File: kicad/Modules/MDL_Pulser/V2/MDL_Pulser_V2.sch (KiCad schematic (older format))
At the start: 1 part

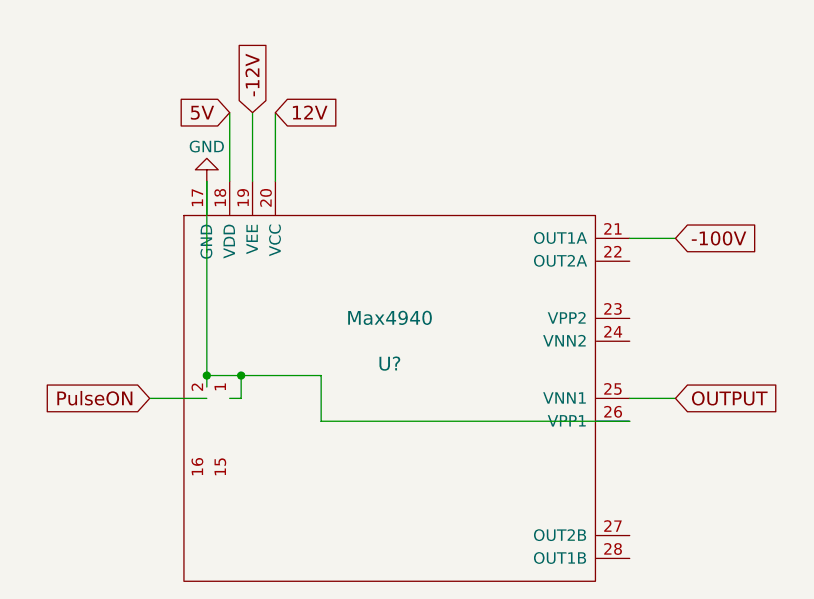
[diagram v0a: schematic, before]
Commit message: adding MDL_Pulser
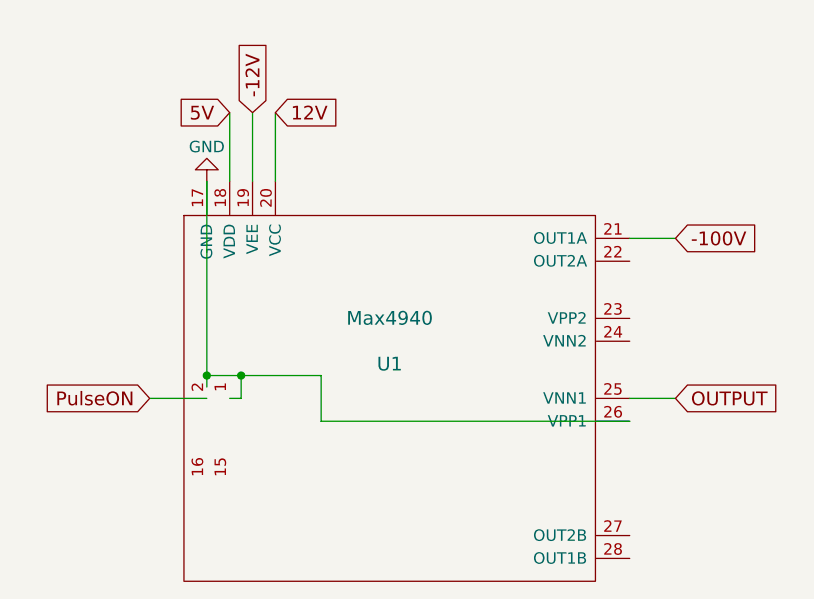
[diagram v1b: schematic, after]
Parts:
- gave numbers to parts that had none: 1
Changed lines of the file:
@@
 $EndDescr
 $Comp
-L Max4940 U?
+L Max4940 U1
 U 1 1 57A315C0
 P 4900 3350
-F 0 "U?" H 4900 3350 60  0000 C CNN
+F 0 "U1" H 4900 3350 60  0000 C CNN
 F 1 "Max4940" H 4900 3550 60  0000 C CNN
 F 2 "" H 4900 3350 60  0000 C CNN
@@
 Connection ~ 4100 3400
 $Comp
-L GND #PWR?
+L GND #PWR01
 U 1 1 57A31671
 P 4100 2550
-F 0 "#PWR?" H 4100 2300 50  0001 C CNN
+F 0 "#PWR01" H 4100 2300 50  0001 C CNN
 F 1 "GND" H 4100 2400 50  0000 C CNN
 F 2 "" H 4100 2550 50  0000 C CNN
